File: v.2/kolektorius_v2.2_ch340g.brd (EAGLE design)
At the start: 100 x 50.2 mm, 87 parts, among them IC1 LM1117-33, IC2 ENC28J60, K1 G5V1, K2 G5V1, K3 G5V1, T1 2N2222, T2 2N2222, T3 2N2222, T4 2N2222, U1 ATMEGA328P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

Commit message: Paliktos 2 reles
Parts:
- removed D1: (no value), adafruit:DO-1N4148
- removed K1: G5V1, relay:G5V1
- removed LED1: (no value), adafruit:1206
- removed R5: 470, rcl:R0805
- removed R6: 3k3, rcl:R0805
- removed T2: 2N2222, adafruit:TO92-EBC-OVAL
- removed X8: 22-23-2031, con-molex:22-23-2031
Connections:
- net D+ renamed N$15
- net D- renamed N$11
- removed net D0: R6.2, U1.30
- removed net N$11 (its old number): D1.A, K1.9, R5.2, T2.C
- removed net N$15 (its old number): K1.10, X8.1
- removed net N$17: R6.1, T2.B
- removed net N$28: K1.5, K1.6, X8.3
- removed net N$29: K1.1, X8.2
- removed net N$31: LED1.C, R5.1
- removed net N$51: U$2.3
- new net RXD: U1.30
- new net TXD: U$2.3, U1.31
- net +5V: no longer D1.C, K1.2, LED1.A
- net D1: no longer U1.31
- net GND: no longer T2.E

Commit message: pataisymai, paliktos 2 reles
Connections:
- removed net D1: X5.2
- net A0: now also X5.2
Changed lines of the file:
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@@
 <signal name="A0">
 <contactref element="U1" pad="23"/>
+<contactref element="X5" pad="2"/>
+<wire x1="25.4" y1="1.905" x2="5.3874" y2="29.34" width="0" layer="19" extent="1-1"/>
 </signal>
 <signal name="A1">
@@
 <contactref element="U1" pad="30"/>
 </signal>
-<signal name="D1">
-<contactref element="X5" pad="2"/>
-</signal>
 <signal name="D8">

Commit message: pataisymai
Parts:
- added R18, R5, R6: 4k7, rcl:R0805
- added U$3: RELAYPTH, SRD-05VDC-SL-C:SRD-05VDC-SL-C
- moved U$2 2.54 mm to (38.1, 12.7)
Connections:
- net +5V: now also R18.1, R5.1, R6.1
- net A0: now also R18.2
- net A1: now also R6.2
- net D2: now also R5.2
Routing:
- net GND: track 0.00 -> 412.3 mm, vias 0 -> 5
- net +5V: track 0.00 -> 290.7 mm, vias 0 -> 5
- net A6: track 0.00 -> 119.0 mm
- net N$46: track 0.00 -> 110.2 mm, vias 0 -> 1
- net A2: track 0.00 -> 101.2 mm, vias 0 -> 3
- net A3: track 0.00 -> 82.4 mm, vias 0 -> 1
- net SCL: track 0.00 -> 73.2 mm, vias 0 -> 1
- net SDA: track 0.00 -> 69.7 mm, vias 0 -> 3
- net D11: track 0.00 -> 64.4 mm, vias 0 -> 2
- net D12: track 0.00 -> 61.1 mm, vias 0 -> 3
- net TXD: track 0.00 -> 51.6 mm
- net D2: track 0.00 -> 50.8 mm
- net A1: track 0.00 -> 47.0 mm, vias 0 -> 3
- net RESET: track 0.00 -> 42.4 mm, vias 0 -> 3
- net RD+: track 0.00 -> 37.2 mm, vias 0 -> 1
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
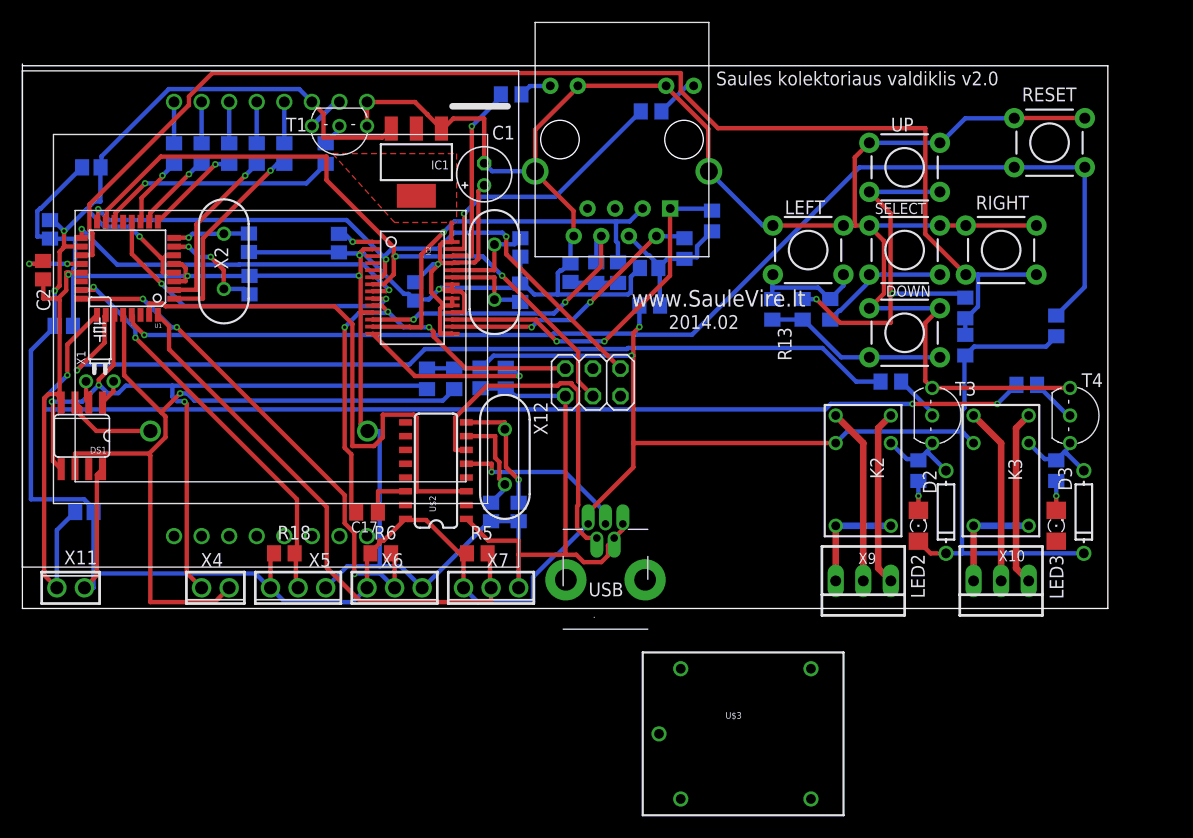
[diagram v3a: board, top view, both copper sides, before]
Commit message: pataisymai
2 reles jrc-21f(4100)
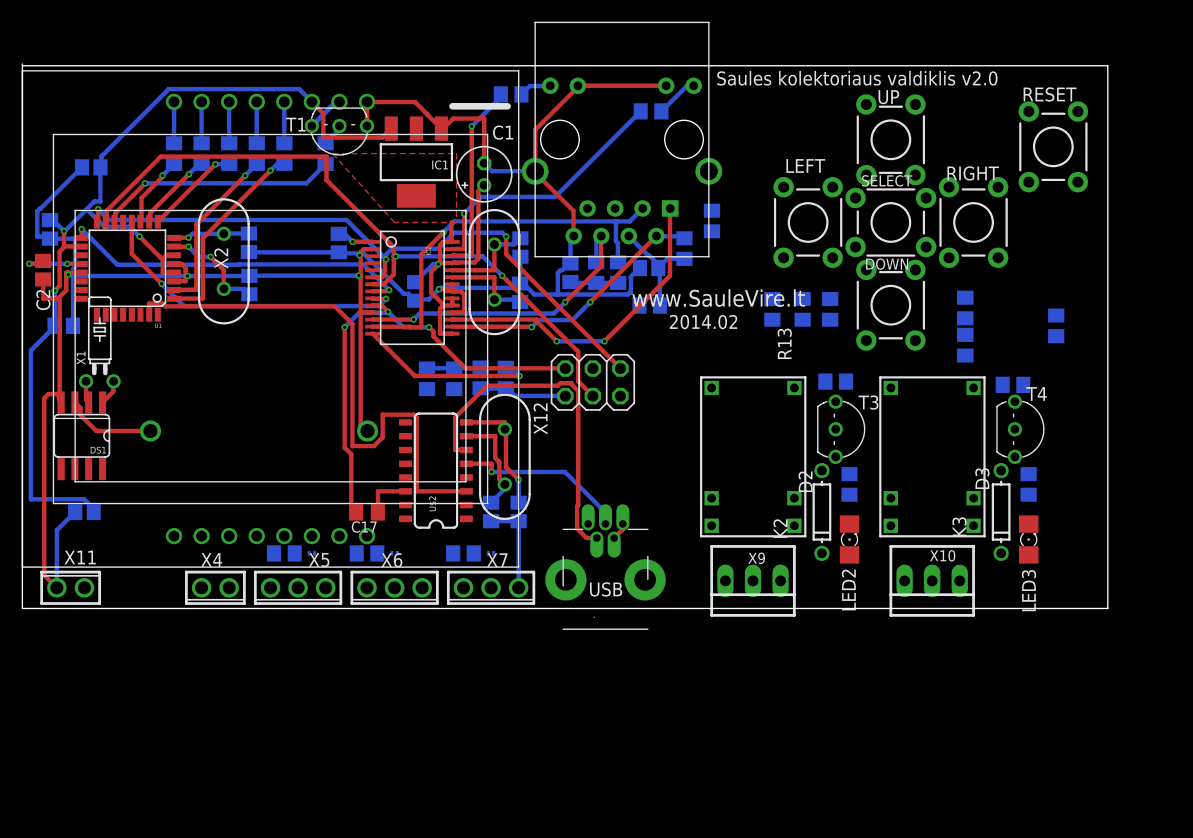
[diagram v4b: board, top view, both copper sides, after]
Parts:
- removed U$3: RELAYPTH, SRD-05VDC-SL-C:SRD-05VDC-SL-C
- added SJ1, SJ2, SJ3: 0R, rcl:R0201
- K3: value G5V1 -> JRC-21F(4100)
- moved D2 11.4 mm to (73.7, 8.89)
- moved X9 10.2 mm to (67.3, 2.54)
- moved T3 8.98 mm to (76.2, 16.5)
- moved K2 8.13 mm to (71.1, 7.62), turned to 90 degrees
- moved D3 7.62 mm to (90.2, 8.89)
- moved LED2 6.48 mm to (76.2, 6.35)
- moved R3 6.48 mm to (76.2, 11.4)
- moved X10 6.35 mm to (83.8, 2.54)
- moved K3 5.68 mm to (87.6, 7.62), turned to 90 degrees
- moved T4 5.24 mm to (92.7, 16.5)
- moved R4 5.08 mm to (74.9, 20.9)
- moved RIGHT 3.59 mm to (87.6, 35.6), turned to 90 degrees
- moved LED3 2.84 mm to (92.7, 6.35)
- moved R1 2.84 mm to (92.7, 11.4)
- moved DOWN 2.84 mm to (80.0, 27.9), turned to 90 degrees
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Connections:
- removed net N$27: LED3.A
- new net N$17: R6.2, SJ2.1
- new net N$28: R18.2, SJ3.1
- new net N$31: R5.2, SJ1.1
- net +5V: now also LED3.A
- net A0: now also SJ3.2; no longer R18.2
- net A1: now also SJ2.2; no longer R6.2
- net D2: now also SJ1.2; no longer R5.2
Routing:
- net +5V: track 290.7 -> 94.4 mm, vias 5 -> 3
- net GND: track 412.3 -> 237.3 mm
- net A6: track 119.0 -> 0.00 mm
- net N$46: track 110.2 -> 0.00 mm, vias 1 -> 0
- net A2: track 101.2 -> 0.00 mm, vias 3 -> 0
- net A3: track 82.4 -> 0.00 mm, vias 1 -> 0
- net SCL: track 73.2 -> 0.00 mm, vias 1 -> 0
- net SDA: track 69.7 -> 0.00 mm, vias 3 -> 0
- net D2: track 50.8 -> 0.00 mm
- net A1: track 47.0 -> 0.00 mm, vias 3 -> 0
- net A0: track 37.1 -> 0.00 mm, vias 2 -> 0
- net N$9: track 35.4 -> 0.00 mm, vias 2 -> 0
- net N$6: track 16.9 -> 0.00 mm
- net N$20: track 16.3 -> 0.00 mm
- net N$5: track 16.3 -> 0.00 mm
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
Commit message: pataisymai
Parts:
- SJ1, SJ2, SJ3: device rcl:R0201 -> rcl:R0402
- moved R5 1.27 mm to (39.4, 5.08)
- moved R18 1.27 mm to (22.9, 5.08)
- moved R6 1.27 mm to (30.5, 5.08)
- flipped SJ1 to the top, turned to 0 degrees
- flipped SJ2 to the top, turned to 0 degrees
- flipped SJ3 to the top, turned to 0 degrees
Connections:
- net N$14: now also K2.1; no longer K2.10
- net N$16: now also X10.2; no longer X10.1
- net N$20: now also X10.1; no longer X10.2
- net N$5: now also K2.10; no longer K2.1
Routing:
- net +5V: track 94.4 -> 333.9 mm, vias 3 -> 6
- net GND: track 237.3 -> 406.4 mm, vias 5 -> 6
- net A6: track 0.00 -> 120.4 mm
- net N$46: track 0.00 -> 118.5 mm, vias 0 -> 3
- net A2: track 0.00 -> 89.2 mm, vias 0 -> 3
- net A3: track 0.00 -> 84.7 mm, vias 0 -> 1
- net SCL: track 0.00 -> 72.4 mm, vias 0 -> 3
- net SDA: track 0.00 -> 67.7 mm, vias 0 -> 3
- net A1: track 0.00 -> 57.7 mm, vias 0 -> 4
- net D2: track 0.00 -> 56.5 mm
- net A0: track 0.00 -> 54.0 mm, vias 0 -> 2
- net N$9: track 0.00 -> 41.1 mm, vias 0 -> 1
- net N$4: track 0.00 -> 28.2 mm
- net N$19: track 0.00 -> 27.0 mm
- net N$6: track 0.00 -> 20.9 mm
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
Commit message: pataisymai, trasavimas
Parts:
- moved C10 4.58 mm to (2.54, 38.1)
- moved R2 2.09 mm to (93.0, 21.8), turned to 90 degrees
- moved K3 1.27 mm to (88.9, 7.62)
- moved LED3 1.27 mm to (94.0, 6.35)
- moved R1 1.27 mm to (94.0, 11.4)
- moved T4 1.27 mm to (94.0, 16.5)
- moved X10 1.27 mm to (85.1, 2.54)
- moved R18 1.27 mm to (22.9, 3.81)
- moved R6 1.27 mm to (30.5, 3.81)
- moved D3 1.27 mm to (91.4, 8.89)
- moved R4 0.90 mm to (75.5, 21.6), turned to 90 degrees
- moved C12 0.90 mm to (1.91, 35.6), turned to 180 degrees
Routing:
- net +5V: track 333.9 -> 305.8 mm
- net A2: track 89.2 -> 101.7 mm, vias 3 -> 4
- net GND: track 406.4 -> 399.9 mm, vias 6 -> 7
- net A3: track 84.7 -> 87.0 mm
- net N$19: track 27.0 -> 28.6 mm

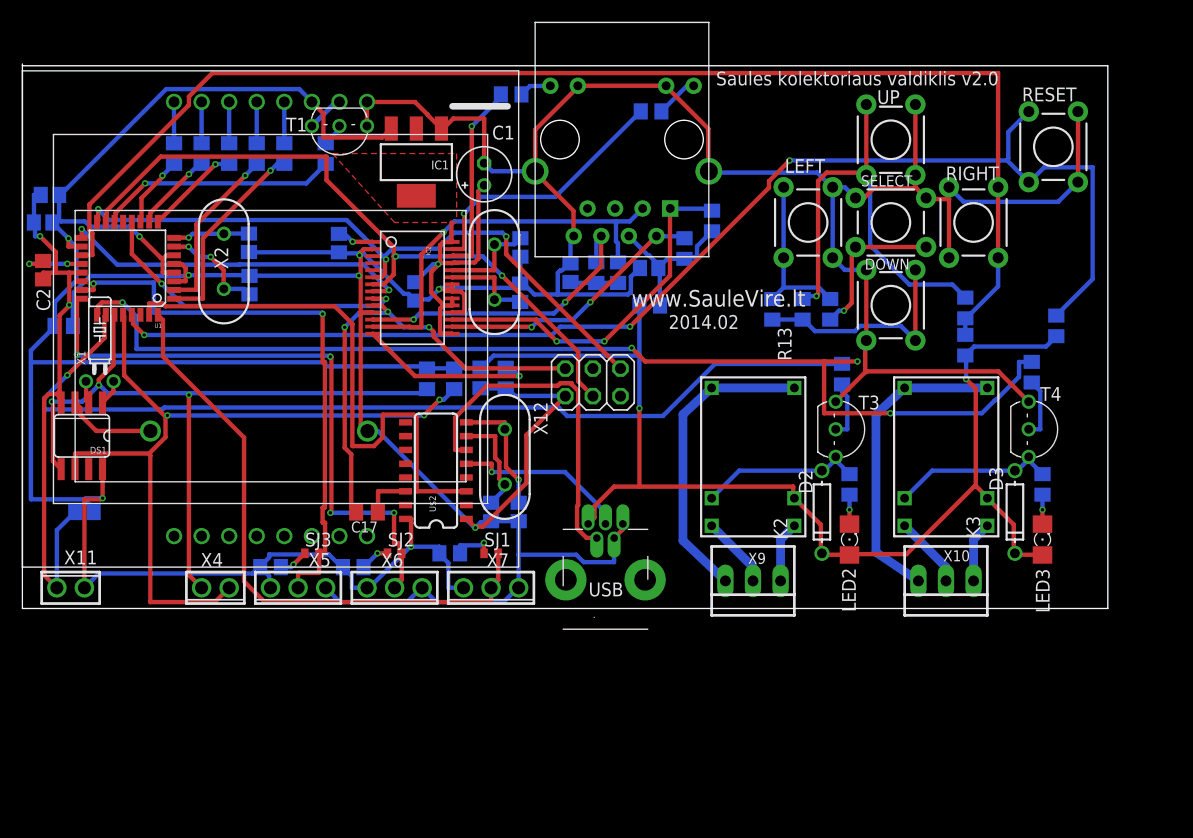
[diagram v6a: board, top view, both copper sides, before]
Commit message: pridėtas  švilpukas
išnaudoti visi kontaktai
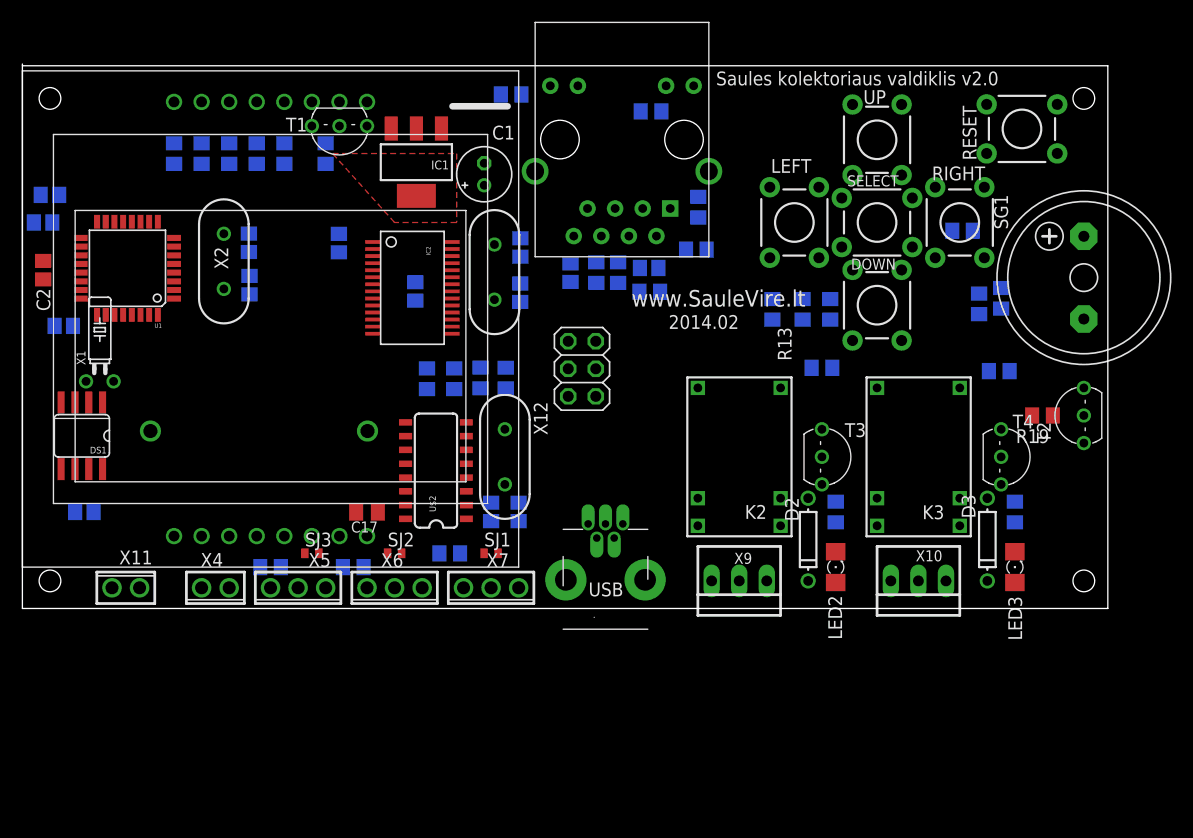
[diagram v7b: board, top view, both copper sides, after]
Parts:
- added R19: 1k, rcl:R0805
- added SG1: F/HMB, buzzer:F/HMB
- added T2: 2N2222, adafruit:TO92-EBC-OVAL
- moved R10 7.12 mm to (86.6, 34.8), turned to 180 degrees
- moved R17 5.68 mm to (90.2, 28.6)
- moved X11 5.08 mm to (9.53, 1.91)
- moved R9 4.02 mm to (88.1, 28.1)
- moved T4 3.59 mm to (91.4, 14.0)
- moved LED3 3.59 mm to (91.4, 3.81)
- moved R1 3.59 mm to (91.4, 8.89)
- moved D3 3.59 mm to (88.9, 6.35)
- moved RESET 3.33 mm to (92.1, 44.2), turned to 0 degrees
- moved R2 3.00 mm to (90.0, 21.9), turned to 0 degrees
- moved D2 2.84 mm to (72.4, 6.35)
- moved T3 2.84 mm to (74.9, 14.0)
- moved LED2 2.84 mm to (74.9, 3.81)
- moved R3 2.84 mm to (74.9, 8.89)
- moved K3 2.54 mm to (86.4, 7.62)
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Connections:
- new net N$27: R19.1, T2.B
- new net N$29: SG1.-, T2.C
- net +5V: now also SG1.+
- net D9: now also R19.2
- net GND: now also T2.E
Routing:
- net GND: track 399.9 -> 0.00 mm, vias 7 -> 0
- net +5V: track 305.8 -> 0.00 mm, vias 6 -> 0
- net A6: track 120.4 -> 0.00 mm
- net N$46: track 118.5 -> 0.00 mm, vias 3 -> 0
- net A2: track 101.7 -> 0.00 mm, vias 4 -> 0
- net A3: track 87.0 -> 0.00 mm, vias 1 -> 0
- net SCL: track 72.4 -> 0.00 mm, vias 3 -> 0
- net SDA: track 67.7 -> 0.00 mm, vias 3 -> 0
- net D11: track 64.4 -> 0.00 mm, vias 2 -> 0
- net D12: track 61.1 -> 0.00 mm, vias 3 -> 0
- net A1: track 57.7 -> 0.00 mm, vias 4 -> 0
- net D2: track 56.5 -> 0.00 mm
- net A0: track 54.0 -> 0.00 mm, vias 2 -> 0
- net TXD: track 51.6 -> 0.00 mm
- net RESET: track 42.4 -> 0.00 mm, vias 3 -> 0
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
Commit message: sutrasuota
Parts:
- moved L1 4.02 mm to (61.6, 27.9)
- moved C4 4.02 mm to (61.5, 30.1)
- moved R15 2.54 mm to (57.4, 30.9)
- moved C5 1.27 mm to (51.8, 30.9)
- moved R16 1.27 mm to (54.1, 30.9)
- moved R10 1.27 mm to (85.9, 35.8), turned to 90 degrees
- turned RIGHT to 270 degrees
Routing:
- net GND: track 0.00 -> 402.0 mm, vias 0 -> 9
- net +5V: track 0.00 -> 303.0 mm, vias 0 -> 5
- net A6: track 0.00 -> 116.2 mm
- net N$46: track 0.00 -> 110.7 mm, vias 0 -> 1
- net A2: track 0.00 -> 93.5 mm, vias 0 -> 5
- net D9: track 0.00 -> 93.3 mm, vias 0 -> 4
- net SDA: track 0.00 -> 82.3 mm, vias 0 -> 2
- net A3: track 0.00 -> 75.2 mm, vias 0 -> 5
- net D12: track 0.00 -> 68.7 mm, vias 0 -> 1
- net SCL: track 0.00 -> 65.6 mm, vias 0 -> 1
- net D11: track 0.00 -> 63.2 mm, vias 0 -> 2
- net A1: track 0.00 -> 58.1 mm, vias 0 -> 2
- net D2: track 0.00 -> 56.1 mm
- net RD+: track 0.00 -> 50.9 mm
- net A0: track 0.00 -> 42.4 mm, vias 0 -> 2
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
